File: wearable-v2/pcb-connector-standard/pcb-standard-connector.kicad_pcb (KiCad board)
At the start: 2 copper layers, 9 x 40 mm, 32 parts, among them J1 HERALD_V2_CONN_RECEPTACLE, J2 HERALD_V2_CONN_RECEPTACLE, J3 HERALD_V2_CONN_RECEPTACLE, J4 HERALD_V2_CONN_RECEPTACLE, J7 USB_C_Receptacle_USB2.0, U1 DT1446-04V, U15 TLV751, U2 MCP73831/2-2MC, U3 TCA6408A, U4 FT201XQ

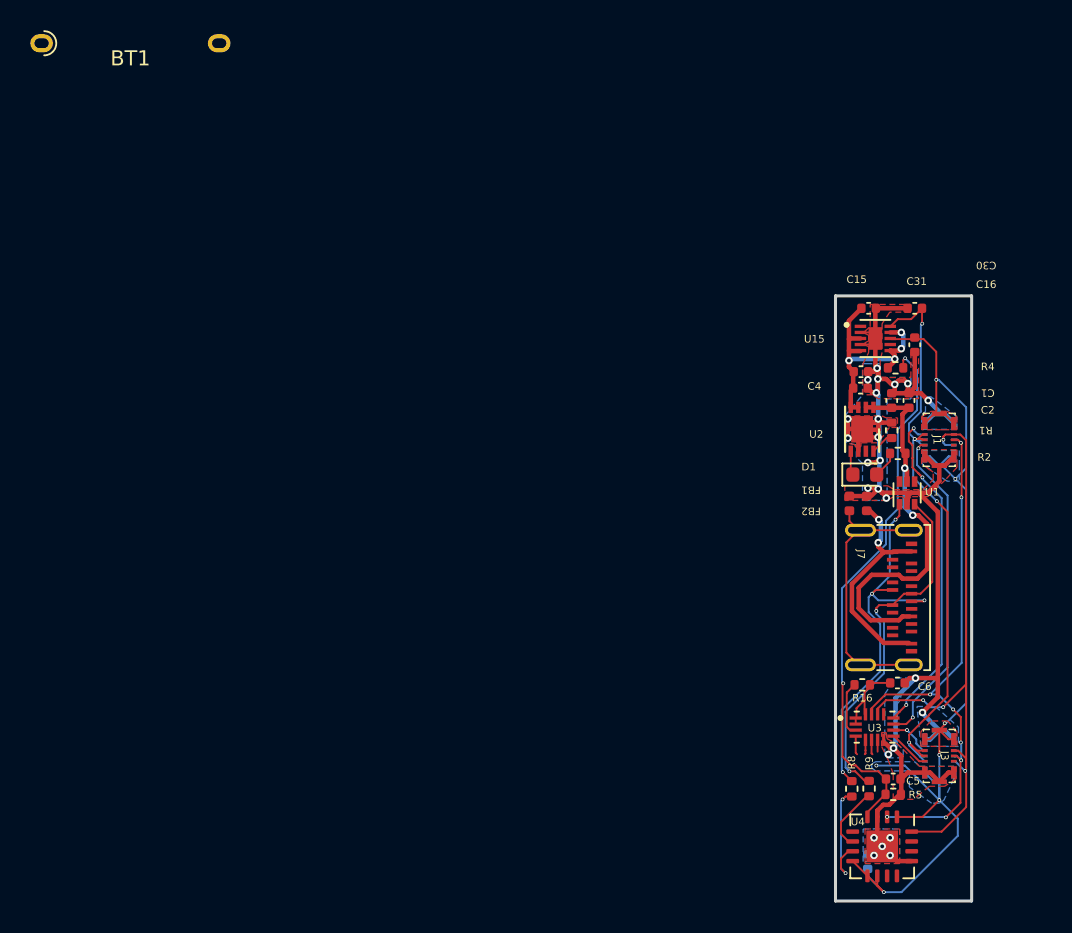
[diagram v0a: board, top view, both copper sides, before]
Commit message: Refactoring PCB files
Moved major boards into their own files.
Corrected design elements for PCBWay manufacture.
Signed-off-by: Adam Fowler <adam@adamfowler.org>
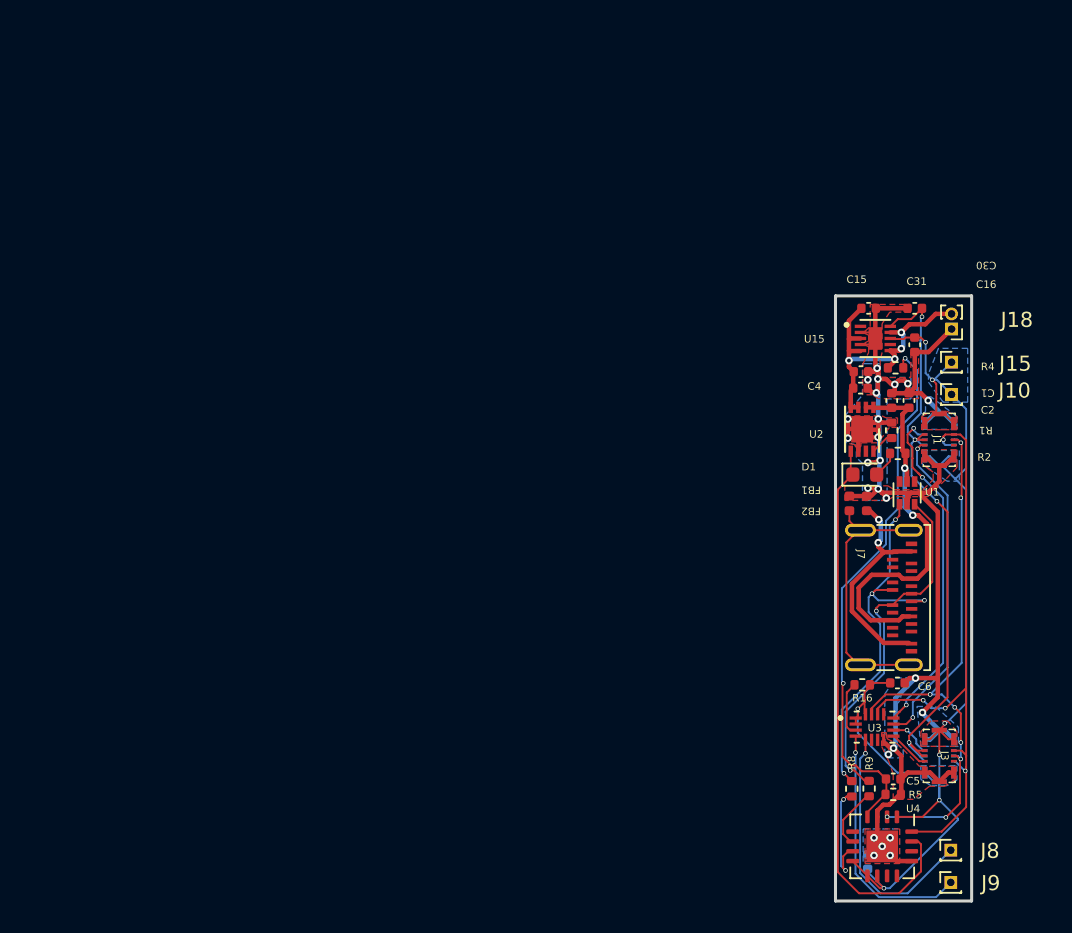
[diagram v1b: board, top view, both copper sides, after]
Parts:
- removed BT1: LiPo, Herald:Herald_Battery_Solder_Pads
- removed ConnectorStandard: Board Standard Connector, PCM_kikit:Board
- added J10: Conn_01x01_Pin, Connector_PinHeader_1.00mm:PinHeader_1x01_P1.00mm_Vertical, F.Cu at (95.8, 103.2)
- added J15: Conn_01x01_Pin, Connector_PinHeader_1.00mm:PinHeader_1x01_P1.00mm_Vertical, F.Cu at (95.8, 101.0)
- added J18: Conn_01x02_Pin, Connector_PinHeader_1.00mm:PinHeader_1x02_P1.00mm_Vertical, F.Cu at (95.8, 98.8)
- added J8: Conn_01x01_Pin, Connector_PinHeader_1.00mm:PinHeader_1x01_P1.00mm_Vertical, F.Cu at (95.7, 133.3)
- added J9: Conn_01x01_Pin, Connector_PinHeader_1.00mm:PinHeader_1x01_P1.00mm_Vertical, F.Cu at (95.7, 135.4)
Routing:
- net /Standard Connector/CH_STAT: track 1.60 -> 37.5 mm
- net /Standard Connector/GPIO_2: track 0.97 -> 16.8 mm, vias 0 -> 1
- net /Standard Connector/GPIO_1: track 1.23 -> 16.5 mm, vias 0 -> 1
- net +BATT: track 16.4 -> 20.2 mm
- net GND: track 99.8 -> 102.8 mm
- net VDD: track 79.2 -> 82.0 mm
- net /Standard Connector/GPIO_3: track 0.97 -> 0.00 mm
- net /Standard Connector/GPIO_4: track 0.78 -> 0.00 mm
- net /Standard Connector/I3C_SCL: track 41.4 -> 40.8 mm
- net Net-(U4-USBDM): track 7.79 -> 7.29 mm
- removed copper zone on B.Cu, net (none)

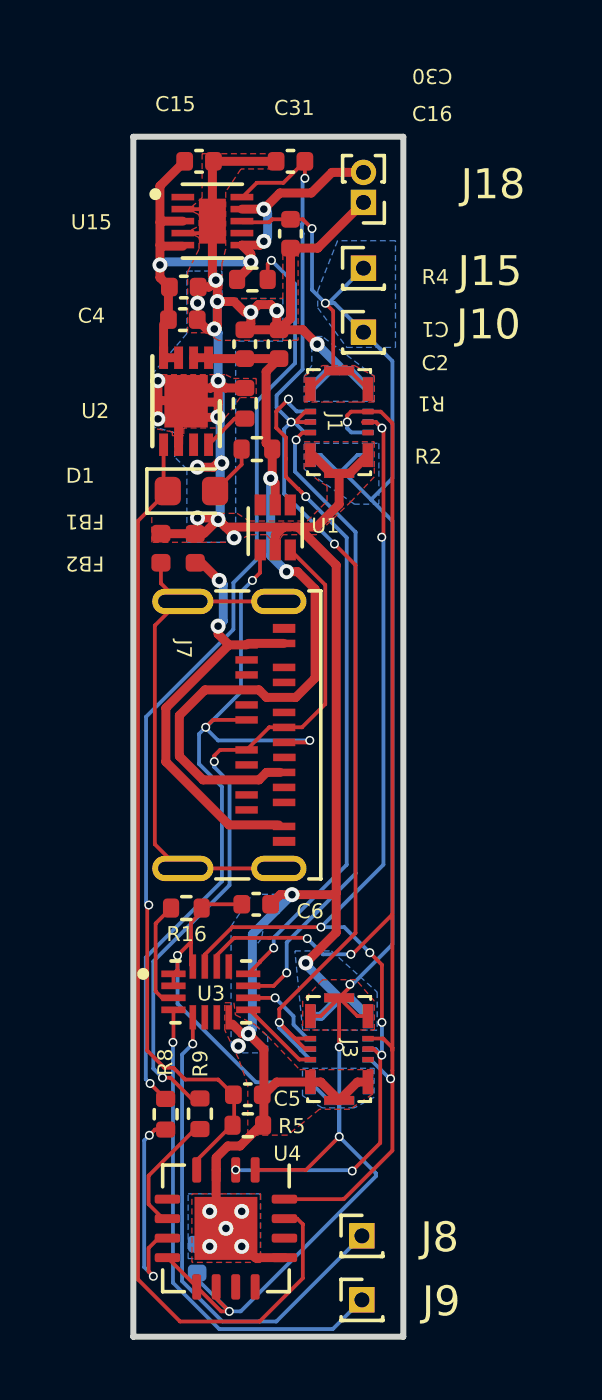
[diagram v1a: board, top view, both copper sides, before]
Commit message: Reworked boards for JLCPCB manufacture
Slightly larger Vias.
Added debug pin holes for Beta testing.
Signed-off-by: Adam Fowler <adam@adamfowler.org>
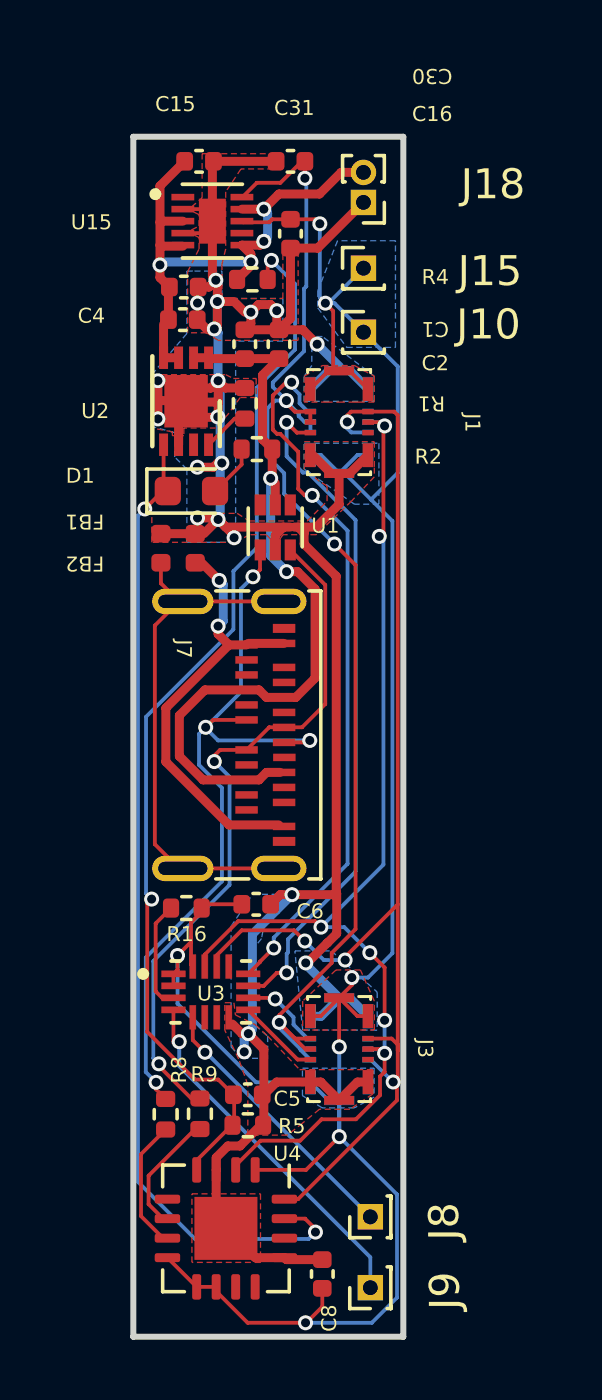
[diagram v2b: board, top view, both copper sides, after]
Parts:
- C8: moved to F.Cu
- moved C8 4.20 mm to (94.4, 134.6)
- moved J8 0.69 mm to (96.0, 132.7), turned to 90 degrees
- moved J9 0.49 mm to (96.0, 135.0), turned to 90 degrees
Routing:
- net /Standard Connector/GPIO_2: track 16.8 -> 9.23 mm
- net /Standard Connector/GPIO_1: track 16.5 -> 11.9 mm
- net /Standard Connector/CH_STAT: track 37.5 -> 33.2 mm, vias 0 -> 2
- net VDD: track 82.0 -> 85.1 mm
- net Net-(U4-USBDM): track 7.29 -> 4.71 mm, vias 2 -> 0
- net GND: track 102.8 -> 104.4 mm, vias 25 -> 20
- net /Standard Connector/INT_2: track 22.7 -> 24.0 mm
- net /Standard Connector/INT_1: track 21.5 -> 22.8 mm
- net +1V8: track 41.0 -> 42.2 mm
- net /Standard Connector/I3C_SCL: track 40.8 -> 41.3 mm
- net /Standard Connector/I3C_SDA: track 38.2 -> 37.9 mm, vias 8 -> 6
